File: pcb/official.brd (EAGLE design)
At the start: 122.9 x 36.9 mm, 27 parts, among them P1 DEV_CLP-150, P11 DEV_1X40

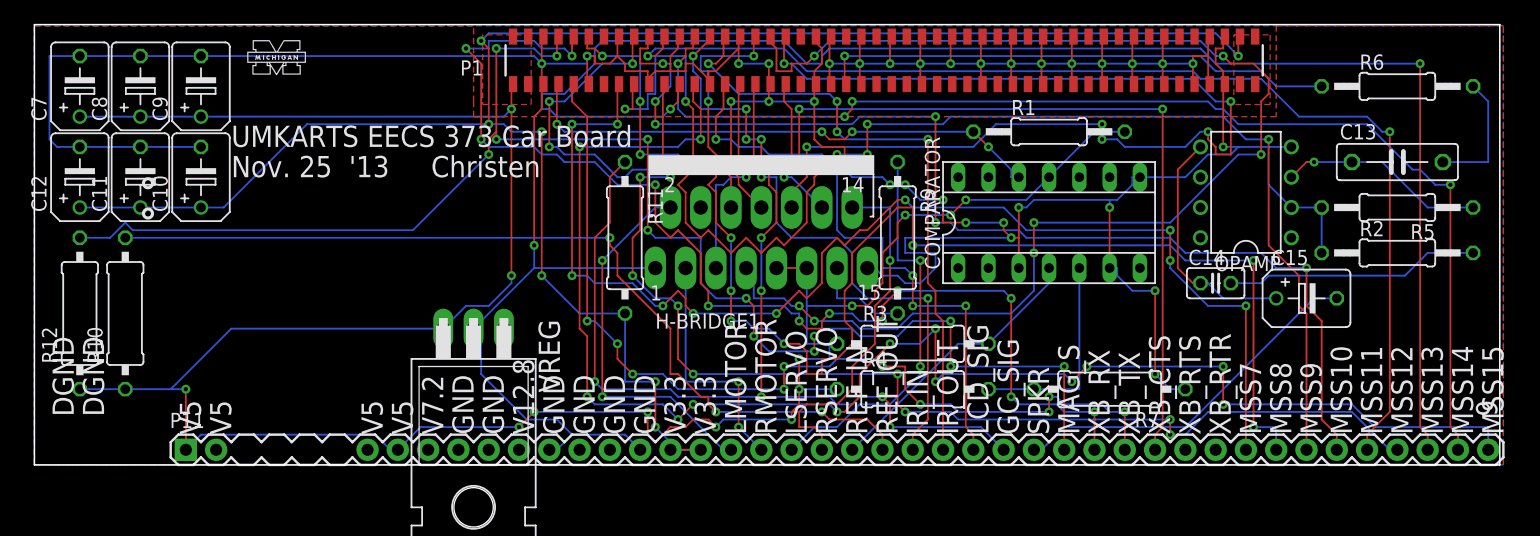
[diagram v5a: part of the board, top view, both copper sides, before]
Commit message: Updated pins and attempt to put layers in eagle
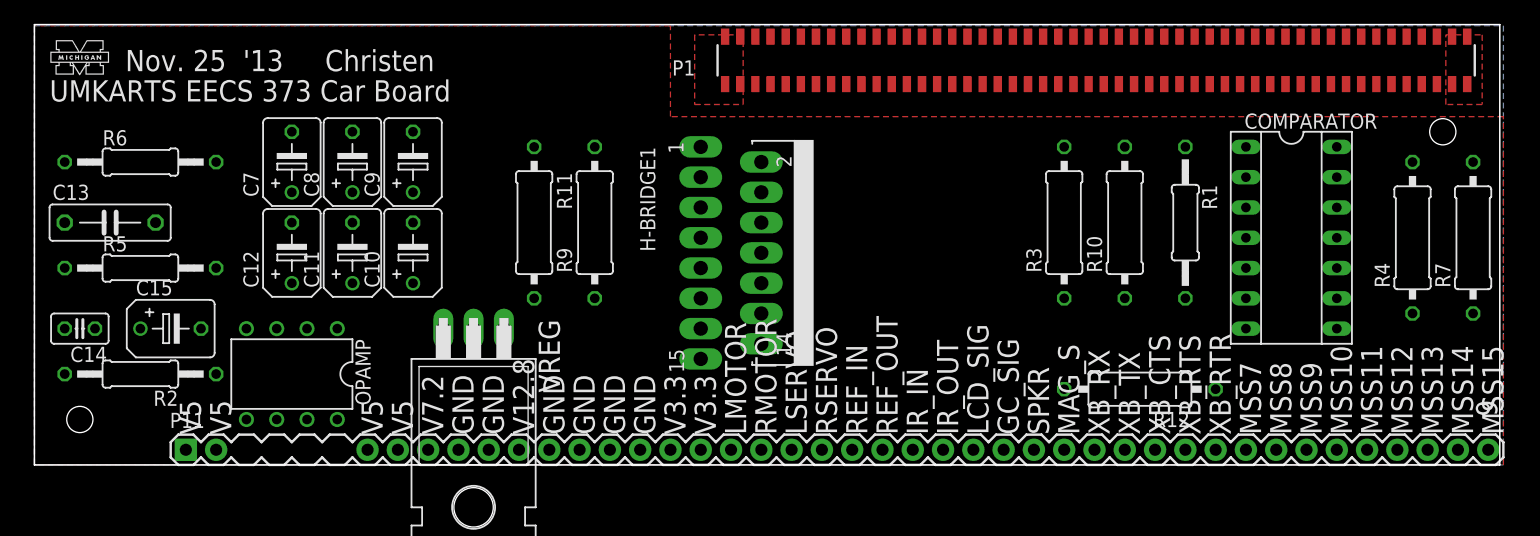
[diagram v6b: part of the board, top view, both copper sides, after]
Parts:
- moved C13 108.1 mm to (6.35, 20.3)
- moved R2 105.9 mm to (8.89, 7.62), turned to 180 degrees
- moved R6 105.6 mm to (8.89, 25.4)
- moved R5 105.5 mm to (8.89, 16.5), turned to 0 degrees
- moved C14 95.3 mm to (3.81, 11.4), turned to 180 degrees
- moved C15 95.3 mm to (11.4, 11.4)
- moved R12 89.1 mm to (92.7, 6.35), turned to 180 degrees
- moved R10 84.2 mm to (91.4, 20.3)
- moved OPAMP 81.4 mm to (21.6, 7.62), turned to 180 degrees
- moved R4 43.8 mm to (115.6, 19.1), turned to 90 degrees
- moved R7 33.0 mm to (120.7, 19.1), turned to 90 degrees
- moved R9 25.4 mm to (47.0, 20.3), turned to 90 degrees
- moved COMPARATOR 20.4 mm to (105.4, 19.1), turned to 270 degrees
- moved C10 18.9 mm to (31.8, 17.8)
- moved C11 18.9 mm to (26.7, 17.8)
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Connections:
- net 12.8V: now also P11.8
- net 7.2V: now also P11.5
- net DGND: now also P11.10, P11.11, P11.6, P11.7
- net VDD5: now also P11.2, P11.3
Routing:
- net DGND: track 305.7 -> 0.00 mm, vias 20 -> 0
- net VDD5: track 217.2 -> 0.00 mm, vias 14 -> 0
- net VDD3.3: track 154.9 -> 0.00 mm, vias 7 -> 0
- net MSS_GP_IO_0: track 130.8 -> 0.00 mm, vias 13 -> 0
- net MSS_GP_IO_15: track 129.1 -> 0.00 mm, vias 13 -> 0
- net MSS_GP_IO_13: track 126.1 -> 0.00 mm, vias 2 -> 0
- net MSS_GP_IO_8: track 123.2 -> 0.00 mm, vias 11 -> 0
- net MSS_GP_IO_9: track 115.6 -> 0.00 mm, vias 6 -> 0
- net F2-200-IO_6: track 109.6 -> 0.00 mm, vias 7 -> 0
- net MSS_GP_IO_7: track 103.3 -> 0.00 mm, vias 10 -> 0
- net MSS_GP_IO_14: track 98.3 -> 0.00 mm, vias 4 -> 0
- net MSS_GP_IO_2: track 98.0 -> 0.00 mm, vias 12 -> 0
- net MSS_GP_IO_12: track 95.8 -> 0.00 mm, vias 9 -> 0
- net MSS_GP_IO_11: track 95.4 -> 0.00 mm, vias 2 -> 0
- net MSS_GP_IO_10: track 92.7 -> 0.00 mm, vias 6 -> 0
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- added copper zone on layer 16, net DGND
- removed copper zone on layer 16, net N$7
- removed copper zone on layer 1, net N$8
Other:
- board text removed: "DGND"

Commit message: Some other pcb stuff
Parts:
- moved H-BRIDGE1 23.2 mm to (40.6, 14.0), turned to 90 degrees
- moved R11 20.9 mm to (62.2, 15.2), turned to 180 degrees
- moved P1 17.8 mm to (71.3, 33.9)
- moved R9 11.4 mm to (58.4, 20.3), turned to 180 degrees
- moved VREG 4.02 mm to (33.0, 0.00)
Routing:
- added copper zone on layer 16, net D$8
- added copper zone on layer 1, net DGND
- removed copper zone on layer 16, net DGND

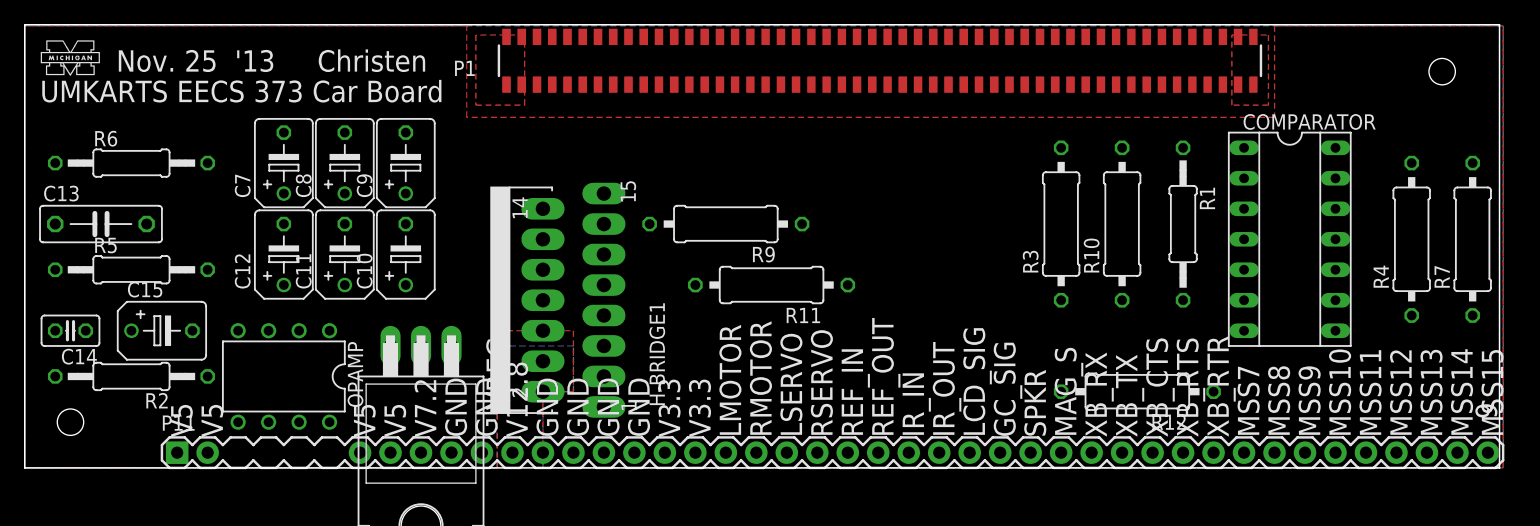
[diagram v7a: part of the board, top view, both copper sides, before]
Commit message: Got rid of delay code
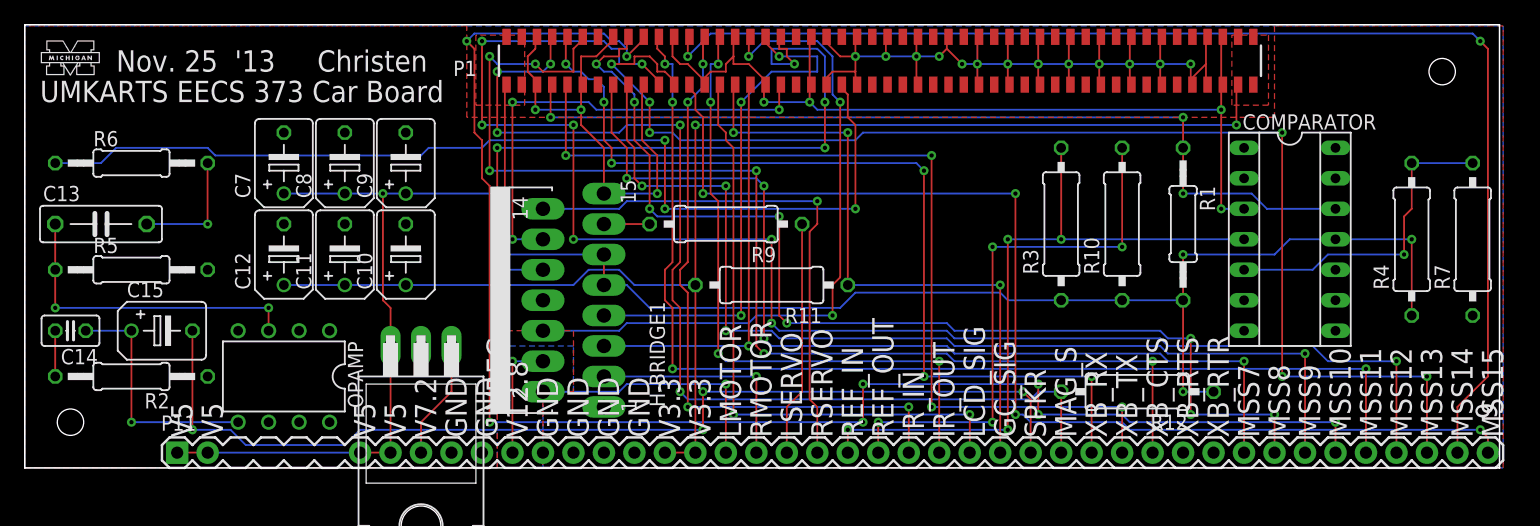
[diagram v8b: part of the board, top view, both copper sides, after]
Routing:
- net VDD5: track 0.00 -> 172.8 mm, vias 0 -> 6
- net MSS_GP_IO_10: track 0.00 -> 128.5 mm, vias 0 -> 8
- net MSS_GP_IO_12: track 0.00 -> 125.8 mm, vias 0 -> 8
- net DGND: track 0.00 -> 117.0 mm, vias 0 -> 7
- net VDD3.3: track 0.00 -> 113.7 mm, vias 0 -> 2
- net MSS_GP_IO_13: track 0.00 -> 106.3 mm, vias 0 -> 6
- net MSS_GP_IO_14: track 0.00 -> 104.4 mm, vias 0 -> 2
- net MSS_GP_IO_4: track 0.00 -> 98.2 mm, vias 0 -> 6
- net MSS_GP_IO_15: track 0.00 -> 95.5 mm, vias 0 -> 4
- net MSS_GP_IO_11: track 0.00 -> 93.9 mm, vias 0 -> 4
- net MSS_GP_IO_8: track 0.00 -> 89.6 mm, vias 0 -> 8
- net MSS_GP_IO_0: track 0.00 -> 87.7 mm, vias 0 -> 5
- net SPKR: track 0.00 -> 87.0 mm, vias 0 -> 4
- net MSS_GP_IO_9: track 0.00 -> 85.4 mm, vias 0 -> 4
- net DACOUT1: track 0.00 -> 84.6 mm, vias 0 -> 3
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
